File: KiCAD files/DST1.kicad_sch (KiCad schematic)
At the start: 58 parts, among them J1 SN49B14B, J2 SN49B14B, J3 Barrel_Jack_MountingPin, J4 Conn_01x03_Pin, J5 Conn_01x03_Pin, J6 Conn_01x03_Pin, Q1 2N3904, Q2 2N3904, Q3 2N3904, U1 TL072

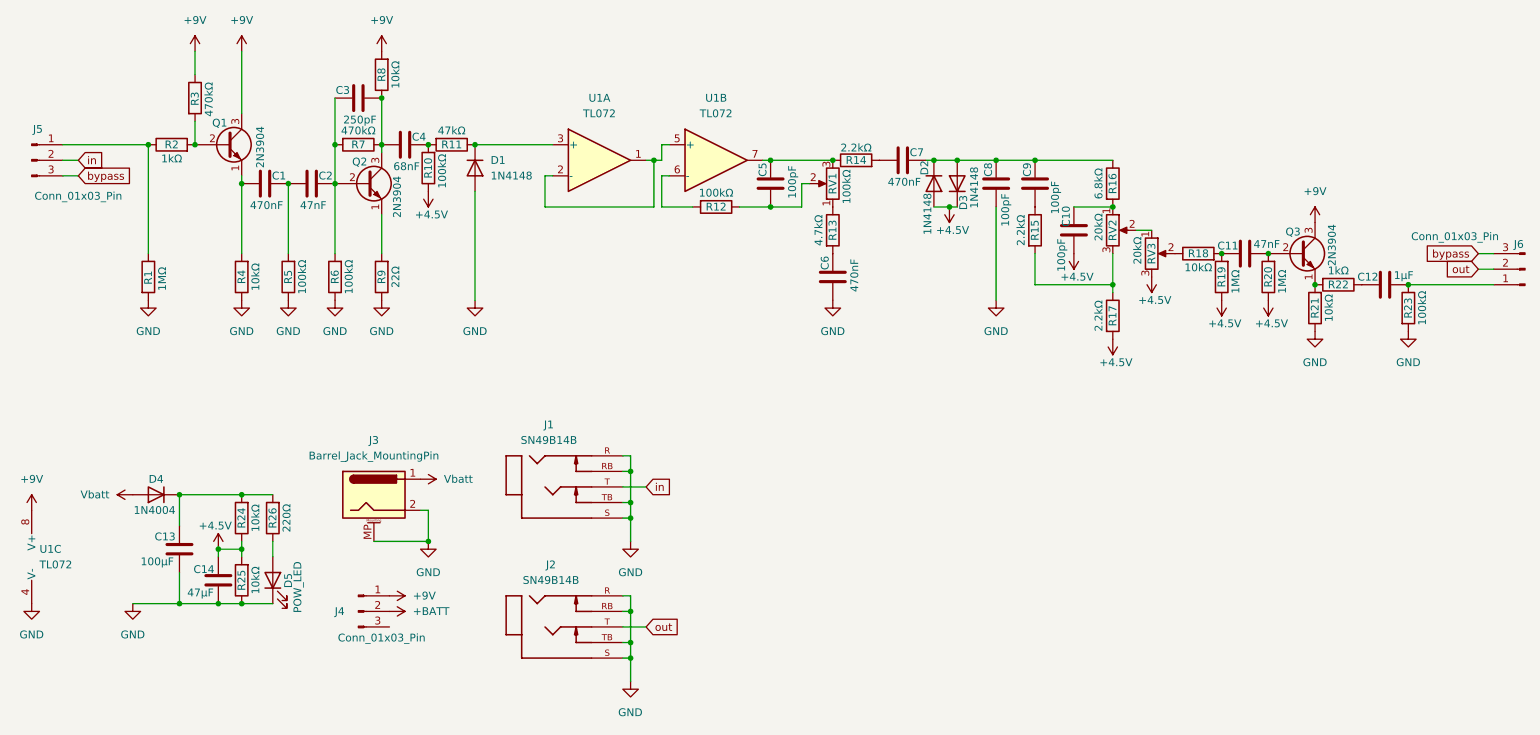
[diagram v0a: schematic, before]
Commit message: Update
I updated the schematic and finished the PCB, might need to upload new photos tho.
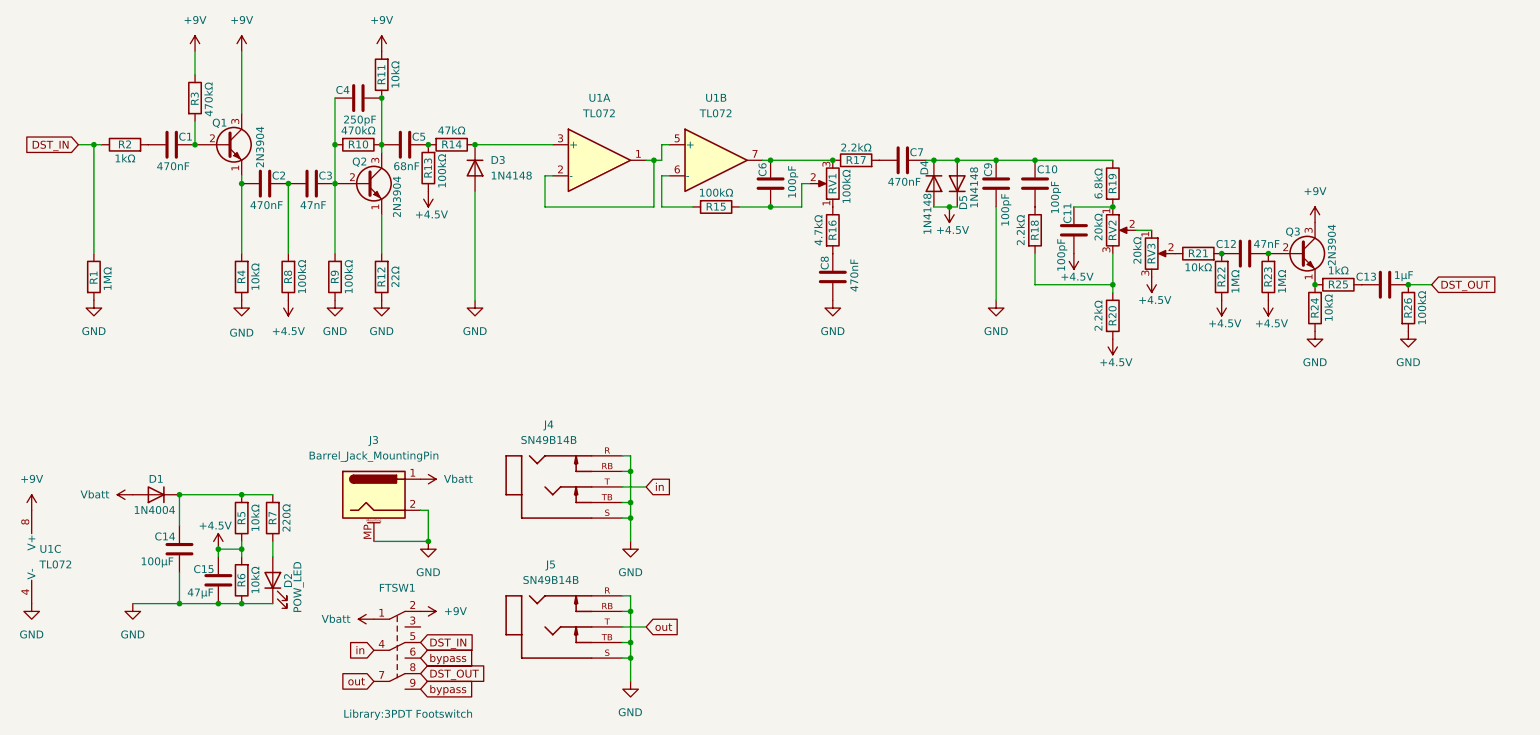
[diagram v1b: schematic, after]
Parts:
- removed J4, J5, J6: Conn_01x03_Pin, Connector_PinHeader_2.54mm:PinHeader_1x03_P2.54mm_Vertical, symbol Connector:Conn_01x03_Pin
- added C1: 470nF, Capacitor_THT:C_Rect_L4.6mm_W3.0mm_P2.50mm_MKS02_FKP02, symbol Device:C
- added FTSW1: ~, Library:3PDT Footswitch, symbol footswitch:3PDT_Footswitch
- renumbered C9 to C10, C10 to C11, C11 to C12, C12 to C13, C13 to C14, C14 to C15, C1 to C2, C2 to C3, C3 to C4, C4 to C5, C5 to C6, C6 to C8, C8 to C9, D4 to D1, D5 to D2, D1 to D3, D2 to D4, D3 to D5, J1 to J4, J2 to J5, R7 to R10, R8 to R11, R9 to R12, R10 to R13, R11 to R14, R12 to R15, R13 to R16, R14 to R17, R15 to R18, R16 to R19, R17 to R20, R18 to R21, R19 to R22, R20 to R23, R21 to R24, R22 to R25, R23 to R26, R24 to R5, R25 to R6, R26 to R7, R5 to R8, R6 to R9
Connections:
- net +4.5V: now also R8.1
- net +9V: now also FTSW1.2
- net GND: no longer R8.1
- net Vbatt: now also FTSW1.1
- net bypass: now also FTSW1.6, FTSW1.9
- net in: now also FTSW1.4
- net out: now also FTSW1.7
- net DST_IN: now reaches R1.1, R2.1
- net DST_IN: now also FTSW1.5
- net at Q1.2 (B), R3.2: now also C1.2; no longer R2.2
- net DST_OUT: now reaches C13.1, R26.1
- net DST_OUT: now also FTSW1.8
- new net: C1.1, R2.2
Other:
- moved on the sheet: R1, R2

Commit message: Updated schematic and PCB
I chose the wrong values for some resistors and capacitors, and so I had to update the schematic. I also wired the footswitch in a wrong manner and so I had to update the PCB.
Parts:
- removed R1: 1MΩ, Resistor_THT:R_Axial_DIN0207_L6.3mm_D2.5mm_P10.16mm_Horizontal, symbol Device:R
- C1: value 470nF -> 47nF
- C10: value 100pF -> 22nF
- C11, C9: value 100pF -> 10nF
- R15: renamed from R20; value 2.2kΩ -> 6.8kΩ
- RV3: value 20kΩ -> 100kΩ
- renumbered C8 to C7, C7 to C8, D3 to D1, D4 to D2, D5 to D3, D1 to D4, D2 to D5, R2 to R1, R14 to R10, R15 to R11, R16 to R12, R17 to R13, R18 to R14, R19 to R16, R21 to R17, R22 to R18, R23 to R19, R3 to R2, R24 to R20, R25 to R21, R26 to R22, R5 to R23, R6 to R24, R7 to R25, R4 to R3, R8 to R4, R9 to R5, R10 to R6, R11 to R7, R12 to R8, R13 to R9
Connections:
- net +4.5V: now also RV3.1; no longer RV3.3
- net at RV2.2: now also RV3.3; no longer RV3.1
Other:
- moved on the sheet: C11, C12, C13, D1, Q3, R15, R16, R17, R18, R19, R2, R20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
